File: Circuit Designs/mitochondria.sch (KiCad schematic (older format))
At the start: 97 parts

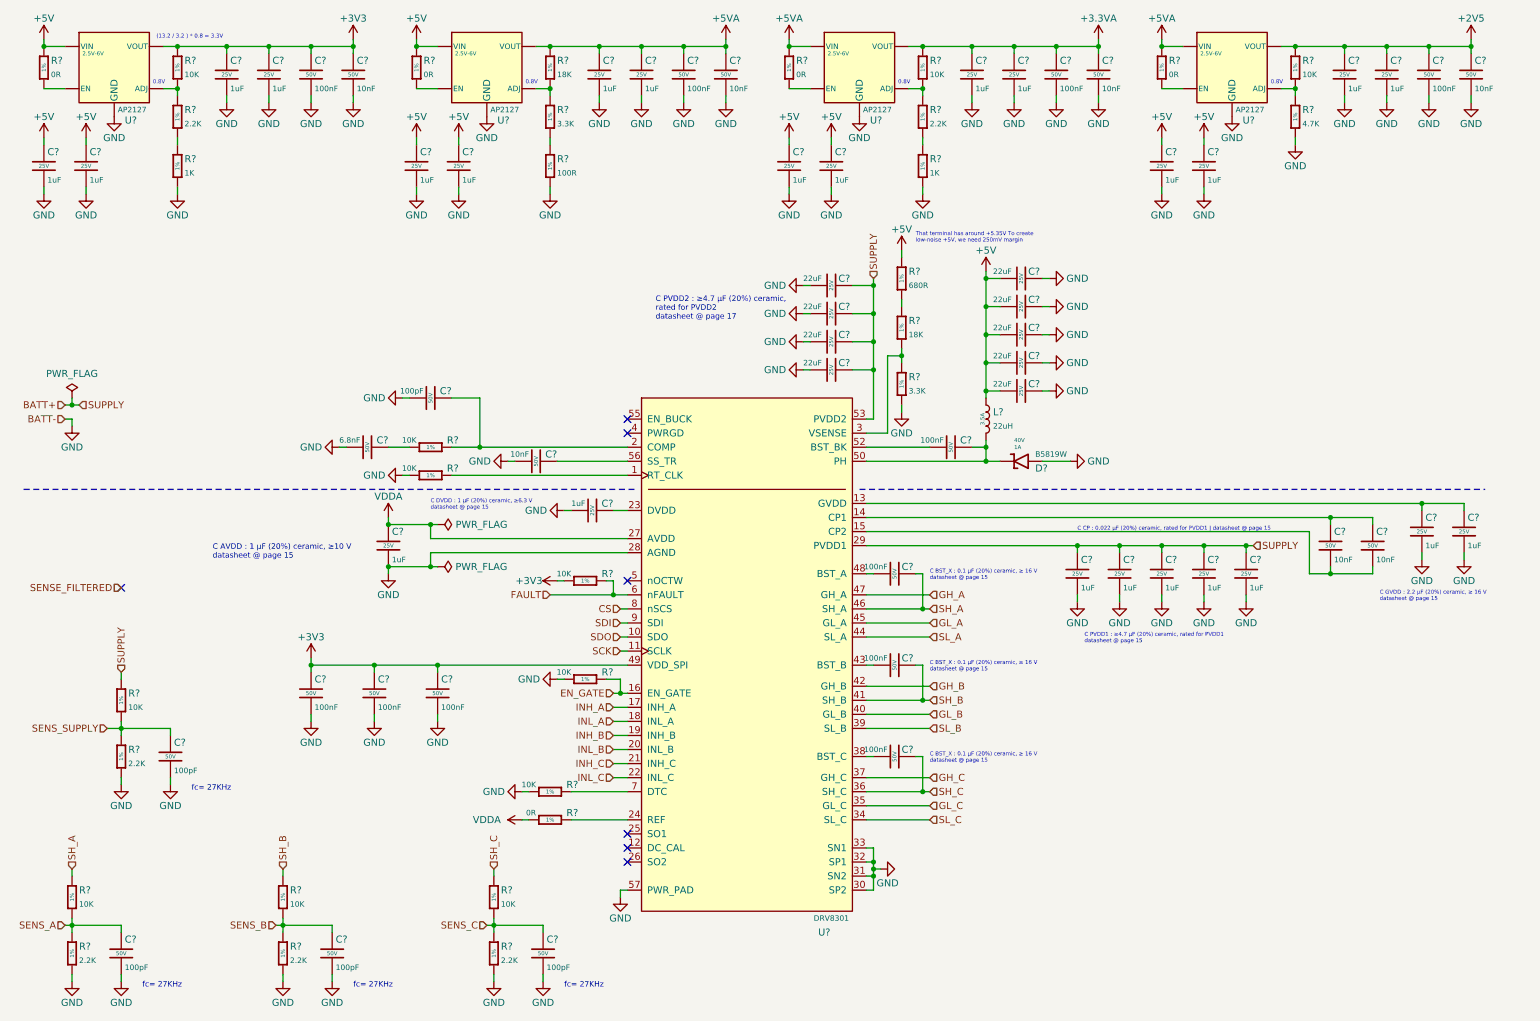
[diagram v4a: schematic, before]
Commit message: edited the buck converter in the motor driver IC
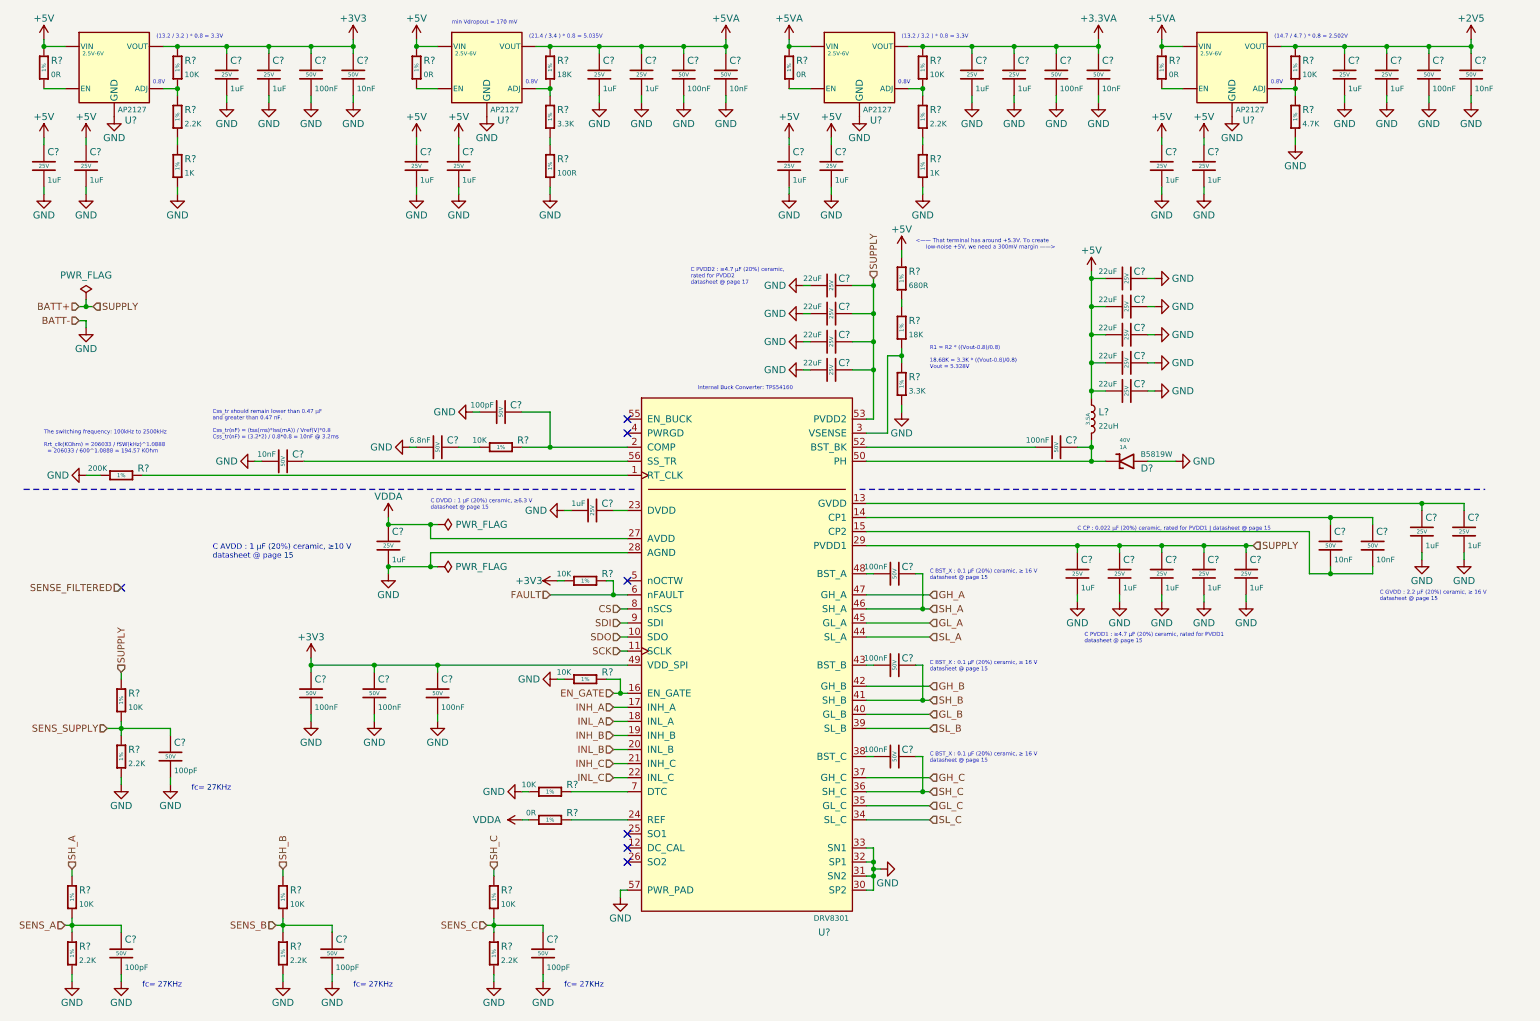
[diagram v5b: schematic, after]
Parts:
- removed R?: 10K, Resistor_SMD:R_0402_1005Metric, symbol CoE_Resistor:10K
- added R?: 200K, Resistor_SMD:R_0402_1005Metric, symbol CoE_Resistor:200K
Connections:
- net GND: now also R?.1
- net at U?.1 (RT_CLK): now also R?.2
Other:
- note added: "(14.7 / 4.7 ) * 0.8 = 2.502V"
- note added: "(21.4 / 3.4 ) * 0.8 = 5.035V"
- note added: "<—— That terminal has around +5.3V. To create \n low-noise +5V, we need a 300mV margin ——>"
- note added: "Css_tr should remain lower than 0.47 μF \nand greater than 0.47 nF.\n\nCss_tr(nF) = (tss(ms)*Iss(mA)) / Vref(V)*0.8\nCss_tr(nF) = (3.2*2) / 0.8*0.8 = 10nF @ 3.2ms"
- note added: "Internal Buck Converter: TPS54160"
- note added: "R1 = R2 * ((Vout-0.8)/0.8)\n\n18.68K = 3.3K * ((Vout-0.8)/0.8)\nVout = 5.328V"
- note added: "The switching frequency: 100kHz to 2500kHz\n\nRrt_clk(KOhm) = 206033 / fSW(kHz)^1.0888 \n = 206033 / 600^1.0888 = 194.57 KOhm"
- note added: "min Vdropout = 170 mV"
- note removed: "That terminal has around +5.35V To create \nlow-noise +5V, we need 250mV margin"
- moved on the sheet: C?, D?, L?, R?

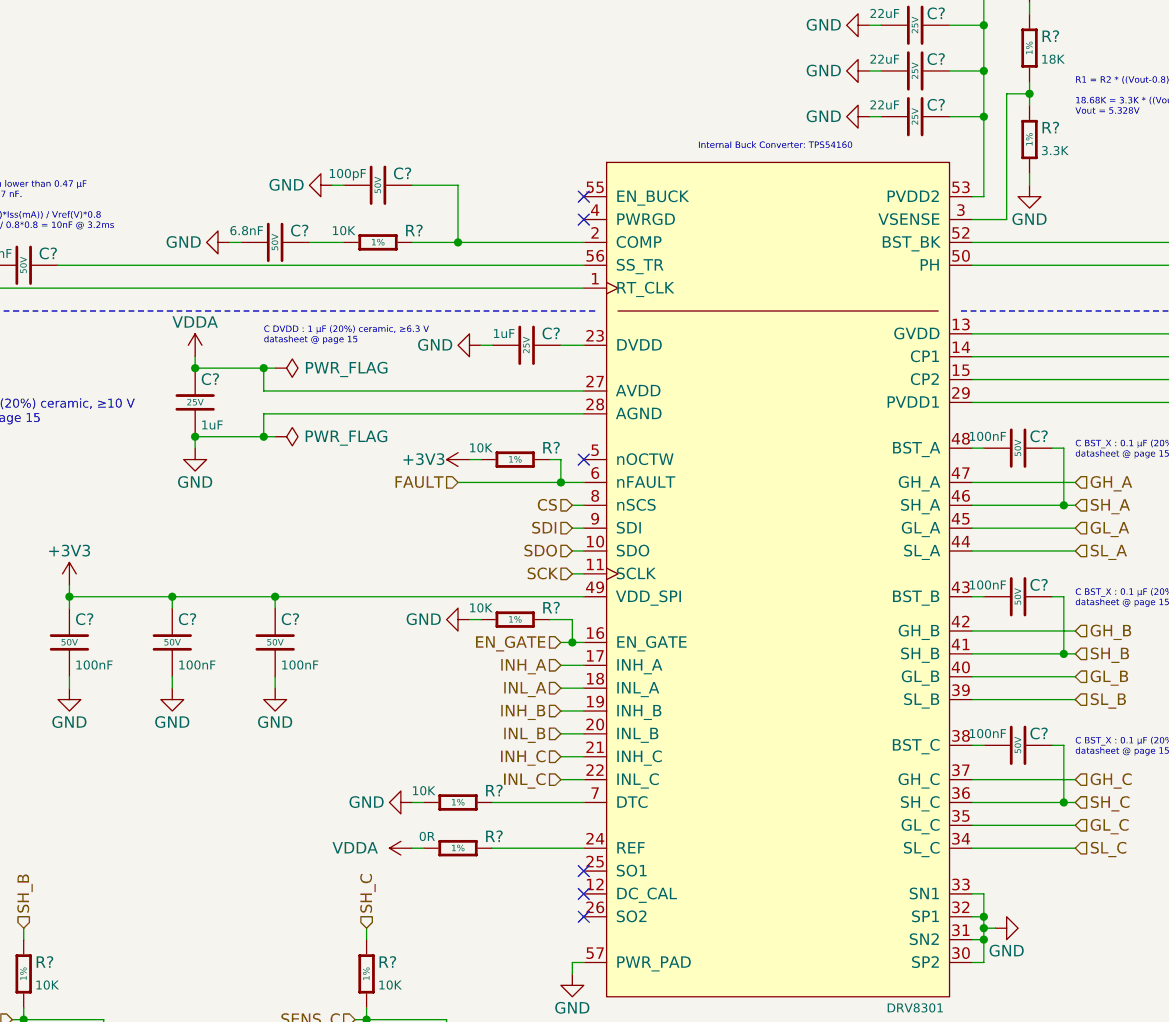
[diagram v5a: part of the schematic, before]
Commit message: tuned the compansation at the buck driver
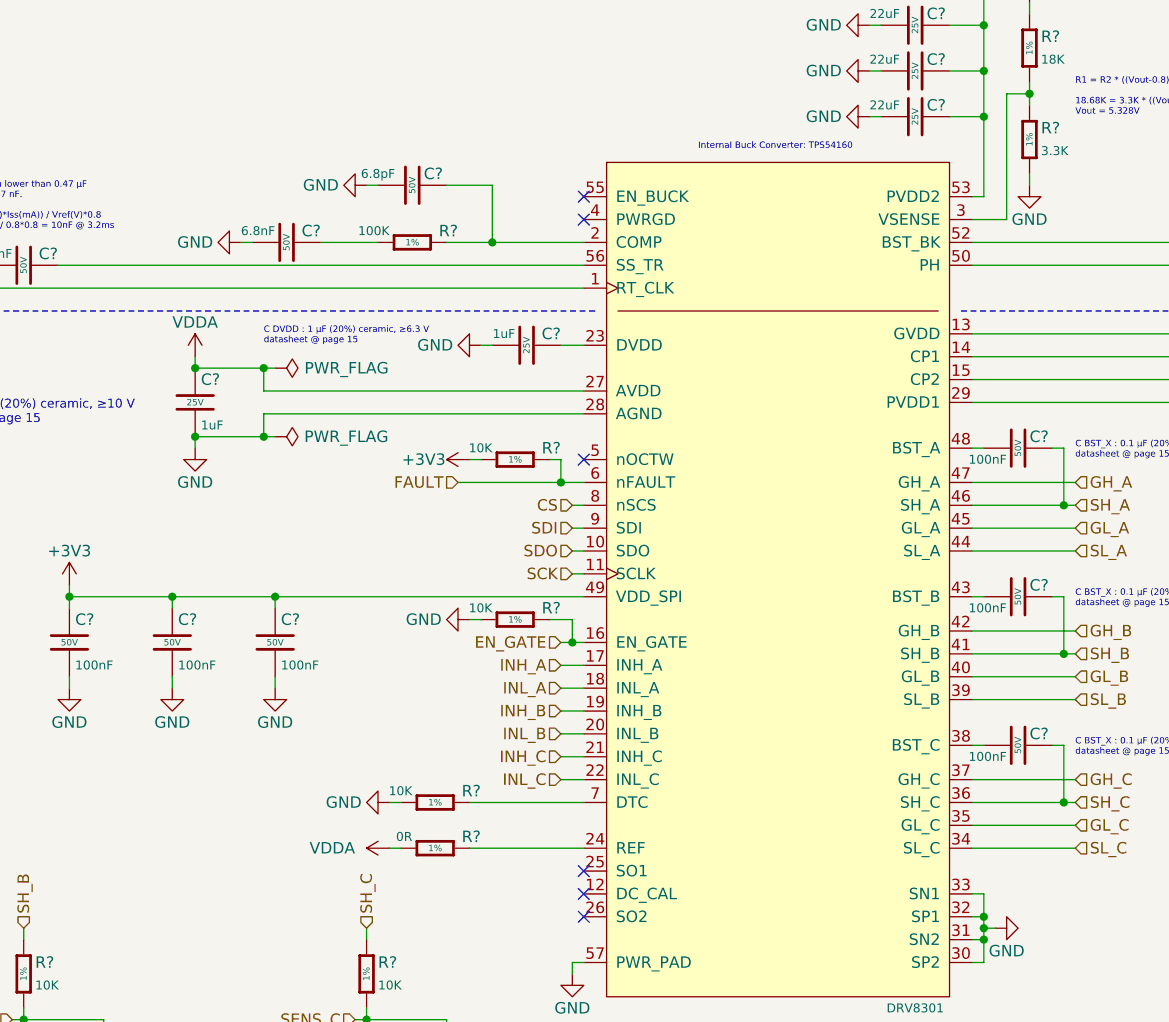
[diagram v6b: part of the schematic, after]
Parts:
- removed C?: 100pF, Capacitor_SMD:C_0402_1005Metric, symbol CoE_Capacitor:100pF
- removed R?: 10K, Resistor_SMD:R_0402_1005Metric, symbol CoE_Resistor:10K
- added C?: 6.8pF, Capacitor_SMD:C_0402_1005Metric, symbol CoE_Capacitor:6.8pF
- added R?: 100K, Resistor_SMD:R_0402_1005Metric, symbol CoE_Resistor:100K
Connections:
- net GND: now also C?.2
- net at C?.2: now also R?.1
- net at U?.2 (COMP): now also C?.1, R?.2
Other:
- moved on the sheet: C?, R?
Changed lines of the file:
@@
 L power:GND #PWR?
 U 1 1 61B426B8
-P 4150 6150
-F 0 "#PWR?" H 4150 5900 50  0001 C CNN
-F 1 "GND" V 4150 5950 50  0000 C CNN
-F 2 "" H 4150 6150 50  0001 C CNN
-F 3 "" H 4150 6150 50  0001 C CNN
-	1    4150 6150
+P 4050 6150
+F 0 "#PWR?" H 4050 5900 50  0001 C CNN
+F 1 "GND" V 4050 5950 50  0000 C CNN
+F 2 "" H 4050 6150 50  0001 C CNN
+F 3 "" H 4050 6150 50  0001 C CNN
+	1    4050 6150
 	0    1    1    0
 $EndComp
 Wire Wire Line
-	4200 6150 4150 6150
+	4100 6150 4050 6150
 $Comp
 L power:VDDA #PWR?
 U 1 1 620C3CC0
-P 4150 6350
-F 0 "#PWR?" H 4150 6200 50  0001 C CNN
-F 1 "VDDA" V 4150 6600 50  0000 C CNN
-F 2 "" H 4150 6350 50  0001 C CNN
-F 3 "" H 4150 6350 50  0001 C CNN
-	1    4150 6350
+P 4050 6350
+F 0 "#PWR?" H 4050 6200 50  0001 C CNN
+F 1 "VDDA" V 4050 6600 50  0000 C CNN
+F 2 "" H 4050 6350 50  0001 C CNN
+F 3 "" H 4050 6350 50  0001 C CNN
+	1    4050 6350
 	0    -1   -1   0
 $EndComp
 Wire Wire Line
-	4200 6350 4150 6350
+	4100 6350 4050 6350
 NoConn ~ 4900 6450
 NoConn ~ 4900 6650
@@
 L power:GND #PWR?
 U 1 1 620C3CC1
-P 3350 3700
-F 0 "#PWR?" H 3350 3450 50  0001 C CNN
-F 1 "GND" V 3350 3500 50  0000 C CNN
-F 2 "" H 3350 3700 50  0001 C CNN
-F 3 "" H 3350 3700 50  0001 C CNN
-	1    3350 3700
+P 3400 3700
+F 0 "#PWR?" H 3400 3450 50  0001 C CNN
+F 1 "GND" V 3400 3500 50  0000 C CNN
+F 2 "" H 3400 3700 50  0001 C CNN
+F 3 "" H 3400 3700 50  0001 C CNN
+	1    3400 3700
 	0    1    1    0
 $EndComp
 Wire Wire Line
-	3350 3700 3400 3700
+	3400 3700 3450 3700
 $Comp
 L power:GND #PWR?
 U 1 1 620C3CC2
-P 3800 3450
-F 0 "#PWR?" H 3800 3200 50  0001 C CNN
-F 1 "GND" V 3800 3250 50  0000 C CNN
-F 2 "" H 3800 3450 50  0001 C CNN
-F 3 "" H 3800 3450 50  0001 C CNN
-	1    3800 3450
+P 3950 3450
+F 0 "#PWR?" H 3950 3200 50  0001 C CNN
+F 1 "GND" V 3950 3250 50  0000 C CNN
+F 2 "" H 3950 3450 50  0001 C CNN
+F 3 "" H 3950 3450 50  0001 C CNN
+	1    3950 3450
 	0    1    1    0
 $EndComp
 Wire Wire Line
-	3800 3450 3850 3450
+	3950 3450 4000 3450
 $Comp
 L power:GND #PWR?
@@
 AR Path="/620004EF/631182B8" Ref="C?"  Part="1"
 F 0 "C?" V 6850 4550 50  0000 R CNN
-F 1 "100nF" V 6850 4650 39  0000 L CNN
+F 1 "100nF" V 6750 4650 39  0000 L CNN
 F 2 "Capacitor_SMD:C_0402_1005Metric" H 6800 5000 50  0001 C BNN
 F 3 "~" H 6800 4600 50  0001 C CNN
@@
 AR Path="/620004EF/6312A025" Ref="C?"  Part="1"
 F 0 "C?" V 6850 5200 50  0000 R CNN
-F 1 "100nF" V 6850 5300 39  0000 L CNN
+F 1 "100nF" V 6750 5300 39  0000 L CNN
 F 2 "Capacitor_SMD:C_0402_1005Metric" H 6800 5650 50  0001 C BNN
 F 3 "~" H 6800 5250 50  0001 C CNN
@@
 AR Path="/620004EF/6312AD54" Ref="C?"  Part="1"
 F 0 "C?" V 6850 5850 50  0000 R CNN
-F 1 "100nF" V 6850 5950 39  0000 L CNN
+F 1 "100nF" V 6750 5950 39  0000 L CNN
 F 2 "Capacitor_SMD:C_0402_1005Metric" H 6800 6300 50  0001 C BNN
 F 3 "~" H 6800 5900 50  0001 C CNN
@@
 $EndComp
 $Comp
-L CoE_Capacitor:100pF C?
-U 1 1 6228C924
-P 4000 3450
-F 0 "C?" V 4050 3300 50  0000 L CNN
-F 1 "100pF" V 4050 3500 39  0000 L CNN
-F 2 "Capacitor_SMD:C_0402_1005Metric" H 4000 3850 50  0001 C BNN
-F 3 "~" H 4000 3450 50  0001 C CNN
-F 4 "50V" H 4000 3450 28  0000 C CNN "Voltage"
-F 5 "0402CG101J500NT" H 4000 3025 50  0001 C CNN "MFR. Part #"
-F 6 "C1546" H 4000 2925 50  0001 C CNN "JLCPCB Part #"
-	1    4000 3450
-	0    -1   -1   0
-$EndComp
-$Comp
 L CoE_Capacitor:10nF C?
 U 1 1 622C3678
@@
 	2250 3800 2300 3800
 $Comp
-L CoE_Capacitor:6.8nF C?
-U 1 1 6230DB94
-P 3550 3700
-F 0 "C?" V 3600 3550 50  0000 L CNN
-F 1 "6.8nF" V 3600 3750 39  0000 L CNN
-F 2 "Capacitor_SMD:C_0402_1005Metric" H 3550 4100 50  0001 C BNN
-F 3 "~" H 3550 3700 50  0001 C CNN
-F 4 "50V" H 3550 3700 28  0000 C CNN "Voltage"
-F 5 "0402B682K500NT" H 3550 3275 50  0001 C CNN "MFR. Part #"
-F 6 "C1542" H 3550 3175 50  0001 C CNN "JLCPCB Part #"
-	1    3550 3700
-	0    -1   -1   0
-$EndComp
-$Comp
 L CoE_Capacitor:100pF C?
 U 1 1 623346C8
@@
 L CoE_Resistor:10K R?
 U 1 1 62A93531
-P 4350 6150
-F 0 "R?" V 4400 5950 50  0000 L CNN
-F 1 "10K" V 4400 6250 39  0000 L CNN
-F 2 "Resistor_SMD:R_0402_1005Metric" H 4350 6550 50  0001 C BNN
-F 3 "~" H 4000 6000 50  0001 C CNN
-F 4 "1%" V 4350 6150 28  0000 C CNN "Tolerance"
-F 5 "0402WGF1002TCE" H 4350 5725 50  0001 C CNN "MFR. Part #"
-F 6 "C25744" H 4350 5625 50  0001 C CNN "JLCPCB Part #"
-	1    4350 6150
+P 4250 6150
+F 0 "R?" V 4300 5950 50  0000 L CNN
+F 1 "10K" V 4300 6250 39  0000 L CNN
+F 2 "Resistor_SMD:R_0402_1005Metric" H 4250 6550 50  0001 C BNN
+F 3 "~" H 3900 6000 50  0001 C CNN
+F 4 "1%" V 4250 6150 28  0000 C CNN "Tolerance"
+F 5 "0402WGF1002TCE" H 4250 5725 50  0001 C CNN "MFR. Part #"
+F 6 "C25744" H 4250 5625 50  0001 C CNN "JLCPCB Part #"
+	1    4250 6150
 	0    -1   -1   0
 $EndComp
-Wire Wire Line
-	4500 6150 4900 6150
 $Comp
 L CoE_Resistor:0R R?
 U 1 1 62ADE5DF
-P 4350 6350
-F 0 "R?" V 4400 6150 50  0000 L CNN
-F 1 "0R" V 4400 6450 39  0000 L CNN
-F 2 "Resistor_SMD:R_0402_1005Metric" H 4350 6750 50  0001 C BNN
-F 3 "~" H 4000 6200 50  0001 C CNN
-F 4 "1%" V 4350 6350 28  0000 C CNN "Tolerance"
-F 5 "0402WGF0000TCE" H 4350 5925 50  0001 C CNN "MFR. Part #"
-F 6 "C17168" H 4350 5825 50  0001 C CNN "JLCPCB Part #"
-	1    4350 6350
+P 4250 6350
+F 0 "R?" V 4300 6150 50  0000 L CNN
+F 1 "0R" V 4300 6450 39  0000 L CNN
+F 2 "Resistor_SMD:R_0402_1005Metric" H 4250 6750 50  0001 C BNN
+F 3 "~" H 3900 6200 50  0001 C CNN
+F 4 "1%" V 4250 6350 28  0000 C CNN "Tolerance"
+F 5 "0402WGF0000TCE" H 4250 5925 50  0001 C CNN "MFR. Part #"
+F 6 "C17168" H 4250 5825 50  0001 C CNN "JLCPCB Part #"
+	1    4250 6350
 	0    -1   -1   0
 $EndComp
-Wire Wire Line
-	4500 6350 4900 6350
 $Comp
 L CoE_Resistor:10K R?
@@
 Wire Wire Line
 	1200 5700 1300 5700
-$Comp
-L CoE_Resistor:10K R?
-U 1 1 6212AF20
-P 4000 3700
-F 0 "R?" V 4050 3500 50  0000 L CNN
-F 1 "10K" V 4050 3800 39  0000 L CNN
-F 2 "Resistor_SMD:R_0402_1005Metric" H 4000 4100 50  0001 C BNN
-F 3 "~" H 3650 3550 50  0001 C CNN
-F 4 "1%" V 4000 3700 28  0000 C CNN "Tolerance"
-F 5 "0402WGF1002TCE" H 4000 3275 50  0001 C CNN "MFR. Part #"
-F 6 "C25744" H 4000 3175 50  0001 C CNN "JLCPCB Part #"
-	1    4000 3700
-	0    -1   -1   0
-$EndComp
 Wire Wire Line
-	3700 3700 3850 3700
-Wire Wire Line
-	4150 3450 4350 3450
+	4300 3450 4500 3450
 $Comp
 L CoE_IntegratedCircuit:DRV8301 U?
@@
 	1050 3900 1150 3900
 Wire Wire Line
-	4150 3700 4350 3700
+	4300 3700 4500 3700
+Wire Wire Line
+	4500 3450 4500 3700
+$Comp
+L CoE_Resistor:100K R?
+U 1 1 621BCD39
+P 4150 3700
+F 0 "R?" V 4200 3500 50  0000 L CNN
+F 1 "100K" V 4200 3800 39  0000 L CNN
+F 2 "Resistor_SMD:R_0402_1005Metric" H 4150 4100 50  0001 C BNN
+F 3 "~" H 3800 3550 50  0001 C CNN
+F 4 "1%" V 4150 3700 28  0000 C CNN "Tolerance"
+F 5 "0402WGF1003TCE" H 4150 3275 50  0001 C CNN "MFR. Part #"
+F 6 "C25741" H 4150 3175 50  0001 C CNN "JLCPCB Part #"
+	1    4150 3700
+	0    -1   -1   0
+$EndComp
+Wire Wire Line
+	4900 3700 4500 3700
+Connection ~ 4500 3700
+Wire Wire Line
+	3750 3700 4000 3700
+$Comp
+L CoE_Capacitor:6.8nF C?
+U 1 1 6230DB94
+P 3600 3700
+F 0 "C?" V 3650 3550 50  0000 L CNN
+F 1 "6.8nF" V 3650 3750 39  0000 L CNN
+F 2 "Capacitor_SMD:C_0402_1005Metric" H 3600 4100 50  0001 C BNN
+F 3 "~" H 3600 3700 50  0001 C CNN
+F 4 "50V" H 3600 3700 28  0000 C CNN "Voltage"
+F 5 "0402B682K500NT" H 3600 3275 50  0001 C CNN "MFR. Part #"
+F 6 "C1542" H 3600 3175 50  0001 C CNN "JLCPCB Part #"
+	1    3600 3700
+	0    -1   -1   0
+$EndComp
+$Comp
+L CoE_Capacitor:6.8pF C?
+U 1 1 62241609
+P 4150 3450
+F 0 "C?" V 4100 3500 50  0000 L CNN
+F 1 "6.8pF" V 4100 3225 39  0000 L CNN
+F 2 "Capacitor_SMD:C_0402_1005Metric" H 4150 3850 50  0001 C BNN
+F 3 "~" H 4150 3450 50  0001 C CNN
+F 4 "50V" H 4150 3450 28  0000 C CNN "Voltage"
+F 5 "0402CG6R8C500NT" H 4150 3025 50  0001 C CNN "MFR. Part #"
+F 6 "C1576" H 4150 2925 50  0001 C CNN "JLCPCB Part #"
+	1    4150 3450
+	0    1    1    0
+$EndComp
 Wire Wire Line
-	4350 3450 4350 3700
-Connection ~ 4350 3700
+	4400 6150 4900 6150
 Wire Wire Line
-	4350 3700 4900 3700
+	4400 6350 4900 6350
 $EndSCHEMATC
